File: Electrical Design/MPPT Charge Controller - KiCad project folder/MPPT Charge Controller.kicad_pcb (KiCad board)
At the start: 4 copper layers, 32 x 80 mm, 75 parts, among them J1 Conn_01x02_Socket, J2 Conn_01x02_Socket, J3 Conn_01x02_Socket, Q1 Q_Dual_NMOS_S1G1S2G2D2D2D1D1, Q2 Q_Dual_NMOS_S1G1S2G2D2D2D1D1, Q3 2N7002, U2 AP63203WU, U3 ACS712, U4 ACS712, U5 MCP4018

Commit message: update PCB for 140K R2
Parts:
- R2: value 499k -> 140K

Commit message: continue to adapt for MEGAphone
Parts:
- removed ? (x3): , 
- removed G***: LOGO, New Logo:byteSizedEngineeringLogo-5mm
- removed J1, J2, J3: Conn_01x02_Socket, TerminalBlock:TerminalBlock_bornier-2_P5.08mm
- removed J4: ~, Connector_PinSocket_2.54mm:PinSocket_1x02_P2.54mm_Vertical
- removed Q2: Q_Dual_NMOS_S1G1S2G2D2D2D1D1, Package_SO:PowerPAK_SO-8_Dual
- removed REF**: MountingHole_3.2mm_M3, MountingHole:MountingHole_3.2mm_M3
- removed TP1, TP10, TP11, TP12, TP13, TP2, TP3, TP4, TP5, TP6, TP7, TP8, TP9: TestPoint, TestPoint:TestPoint_Pad_D1.0mm
- removed TP14, TP15: TestPoint, TestPoint:TestPoint_Loop_D2.60mm_Drill1.6mm_Beaded
- added JP1: Jumper_2_Bridged, Jumper:SolderJumper-2_P1.3mm_Bridged_RoundedPad1.0x1.5mm, F.Cu at (103.1, 77.3)
- added JP2: Jumper_2_Bridged, Jumper:SolderJumper-2_P1.3mm_Bridged_RoundedPad1.0x1.5mm, F.Cu at (103.0, 111.9)
- added M2: ~, MegaCastle:MegaCastle2x23-Module-I30.0x53.6-M80000307FFFC, F.Cu at (110.4, 99.3)
- RSR1: value 0.02 -> 0.01
- moved D3 12.8 mm to (98.0, 119.8)
- moved D4 12.8 mm to (96.0, 119.7)
- moved R7 12.8 mm to (98.0, 119.8)
- moved R8 12.8 mm to (96.0, 119.7)
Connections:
- net Net-(J2-Pin_2) renamed VBAT_OUT
- net PWR GND renamed PWR_GND
- A1 pad 14: unconnected-(A1-RX/IO16-Pad14) -> UART_RX
- A1 pad 15: unconnected-(A1-TX/IO17-Pad15) -> UART_TX
- A1 pad 23: /Load Enable -> unconnected-(A1-D11-Pad23)
- R11 pad 2: +3.3V -> VCC_ACS712_2
- R14 pad 2: +3.3V -> VCC_ACS712
- U3 pad 8: +3.3V -> VCC_ACS712
- U4 pad 8: +3.3V -> VCC_ACS712_2
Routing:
- net +3.3V: track 83.5 -> 139.6 mm
- net VBAT_OUT: track 1.91 -> 56.7 mm
- net UART_RX: track 0.00 -> 47.1 mm, vias 0 -> 1
- net UART_TX: track 0.00 -> 34.9 mm, vias 0 -> 2
- net /Load Enable: track 21.6 -> 0.00 mm, vias 2 -> 0
- net /STAT2: track 97.3 -> 77.3 mm, vias 6 -> 4
- net PWR_GND: track 16.2 -> 33.3 mm
- net /STAT1: track 88.0 -> 73.6 mm, vias 6 -> 2
- net /~{Charge EN}: track 19.3 -> 27.6 mm
- net /VREF: track 55.3 -> 47.4 mm, vias 7 -> 5
- net /HIDRV: track 23.6 -> 30.0 mm, vias 3 -> 2
- net /MPPSET: track 31.6 -> 37.4 mm, vias 4 -> 3
- net /LODRV: track 22.4 -> 28.2 mm, vias 3 -> 2
- net /BTST: track 22.2 -> 28.0 mm, vias 4 -> 3
- net /RGEN: track 20.0 -> 25.6 mm, vias 5 -> 4
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- removed copper zone on F.Cu, net Net-(J3-Pin_1)
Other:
- board size 32 x 80 mm -> 35.6 x 58.4 mm
- board text added: "3.3V OUT"
- board text added: "BATTERY (LiFePO4 1S)"
- board text added: "PWR GND"
- board text added: "UART RX"
- board text added: "UART TX"
- board text removed: "- + 12V Battery"
- board text removed: "- + 12V Load"
- board text removed: "- + 5V-28V Solar Input"

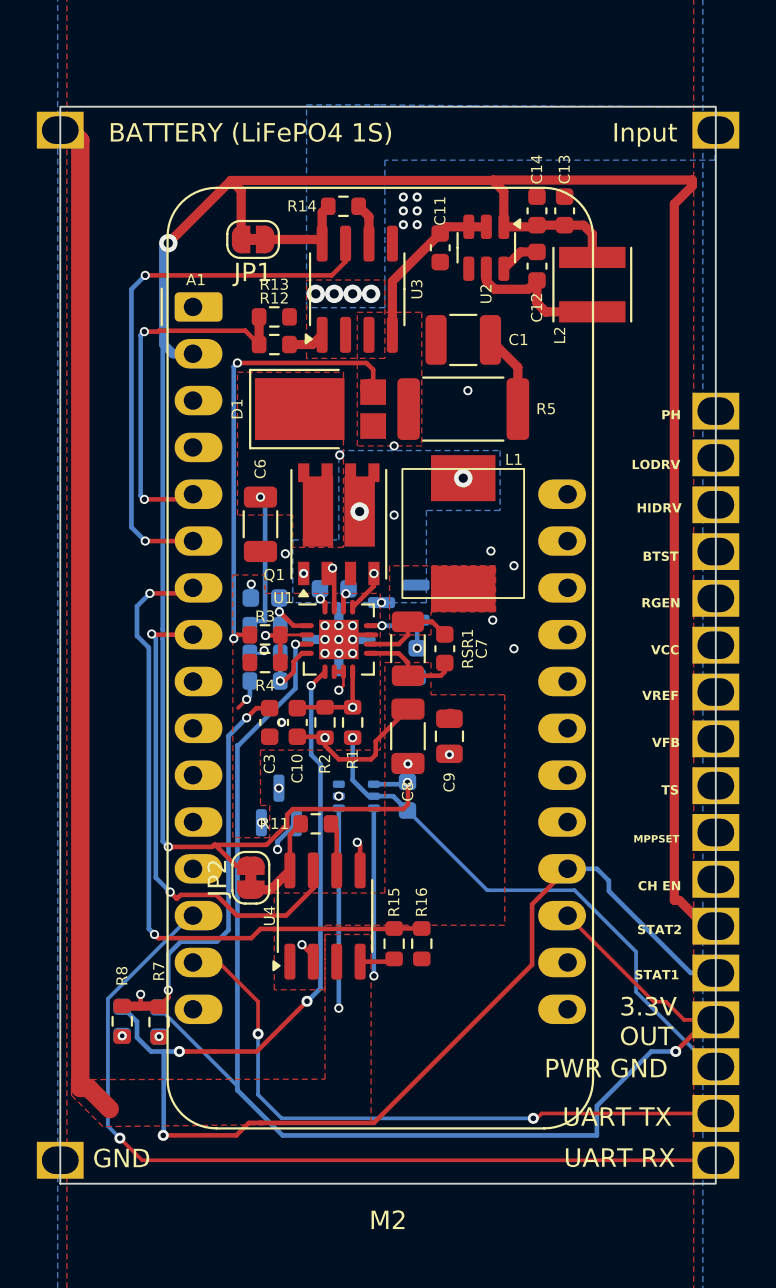
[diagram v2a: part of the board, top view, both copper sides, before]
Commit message: resolve most DRC violations
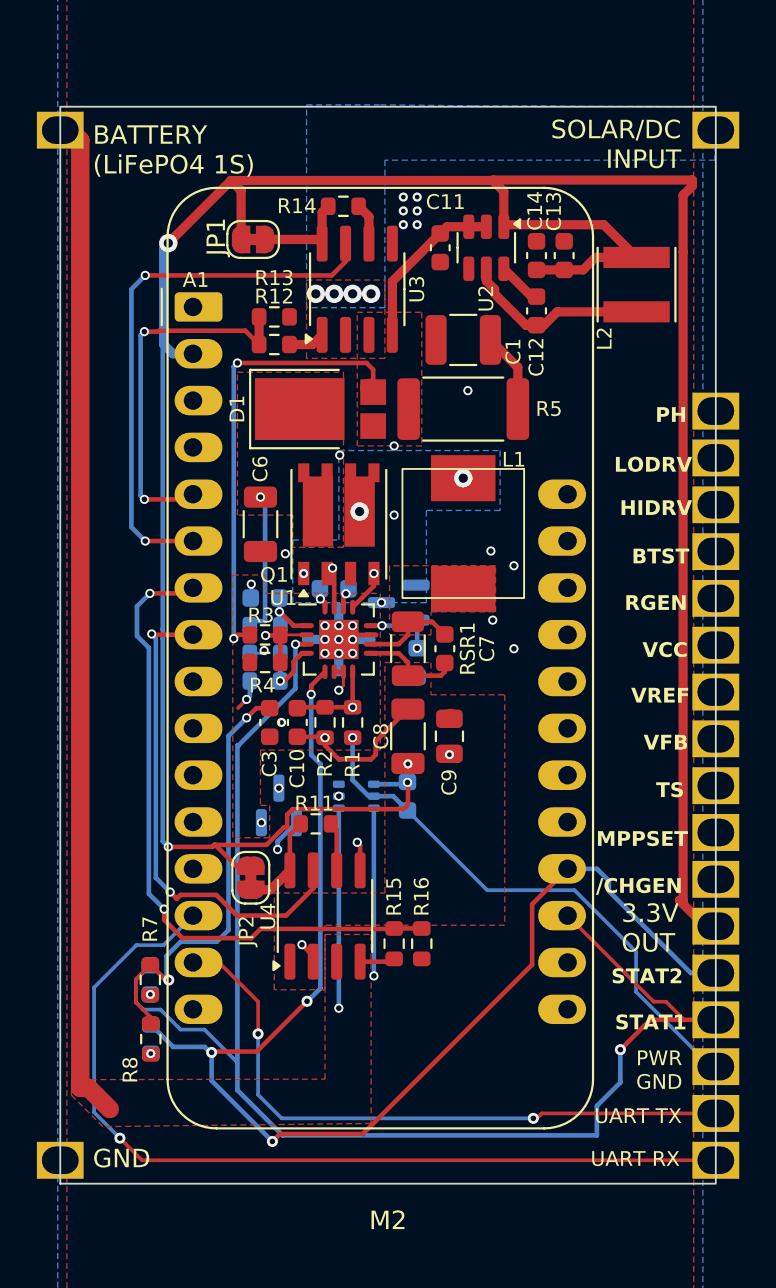
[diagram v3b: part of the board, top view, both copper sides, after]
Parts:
- R5: value 2 -> 2 Ohm
- moved C12 2.43 mm to (118.5, 81.2)
- moved C13 2.43 mm to (120.0, 78.2)
- moved C14 2.43 mm to (118.5, 78.2)
- moved L2 2.40 mm to (123.9, 79.8)
- moved D3 2.34 mm to (97.5, 117.5)
- moved R7 2.34 mm to (97.5, 117.5)
- moved D4 1.82 mm to (97.5, 120.7)
- moved R8 1.82 mm to (97.5, 120.7)
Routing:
- net +3.3V: track 139.6 -> 147.2 mm
- net /STAT2: track 77.3 -> 70.1 mm
- net /STAT1: track 73.6 -> 79.1 mm
- net Net-(U2-SW): track 8.24 -> 10.3 mm
- net UART_RX: track 47.1 -> 48.6 mm
- net /VREF: track 47.4 -> 48.5 mm, vias 5 -> 4
- net /Battery Voltage: track 36.4 -> 35.7 mm
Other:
- board text added: "/CHGEN"
- board text added: "SOLAR/DC INPUT"
- board text removed: "CH EN"
- board text removed: "Input"

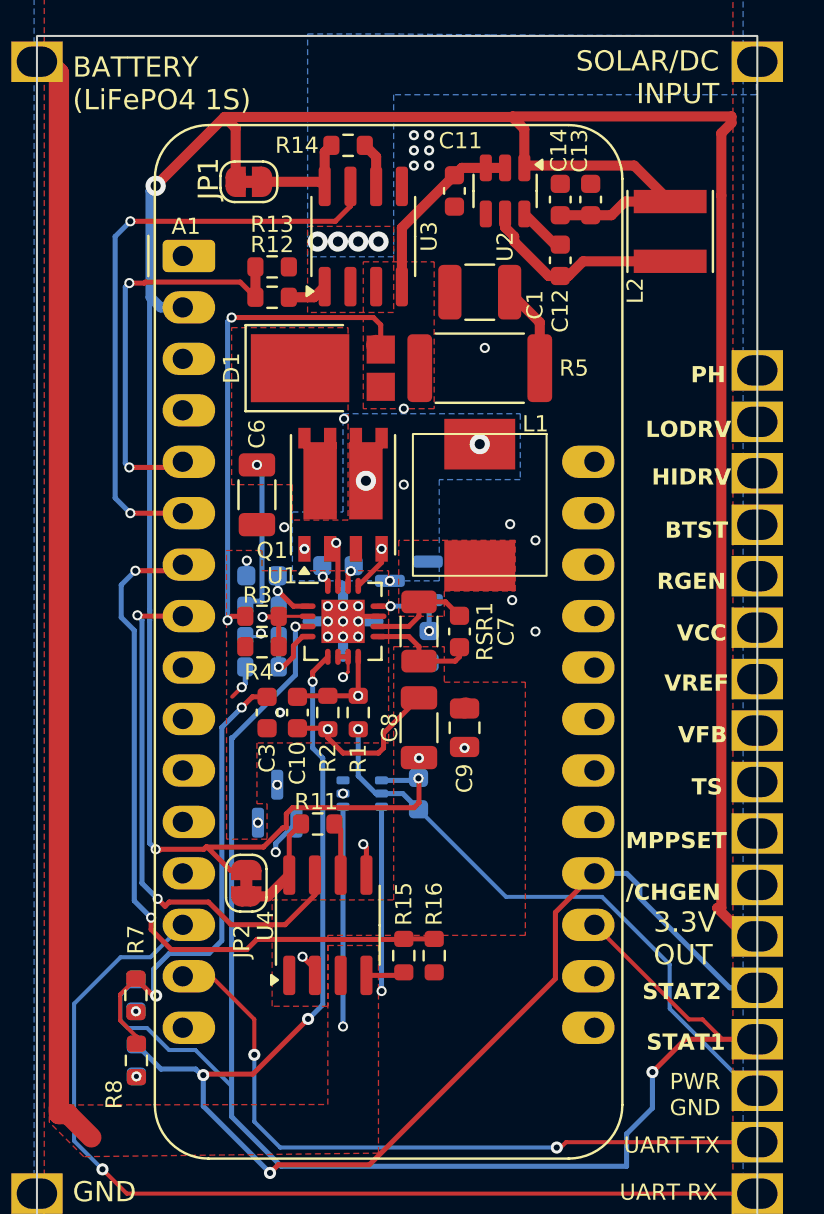
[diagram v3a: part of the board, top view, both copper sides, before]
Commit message: add silkscreen for all component values
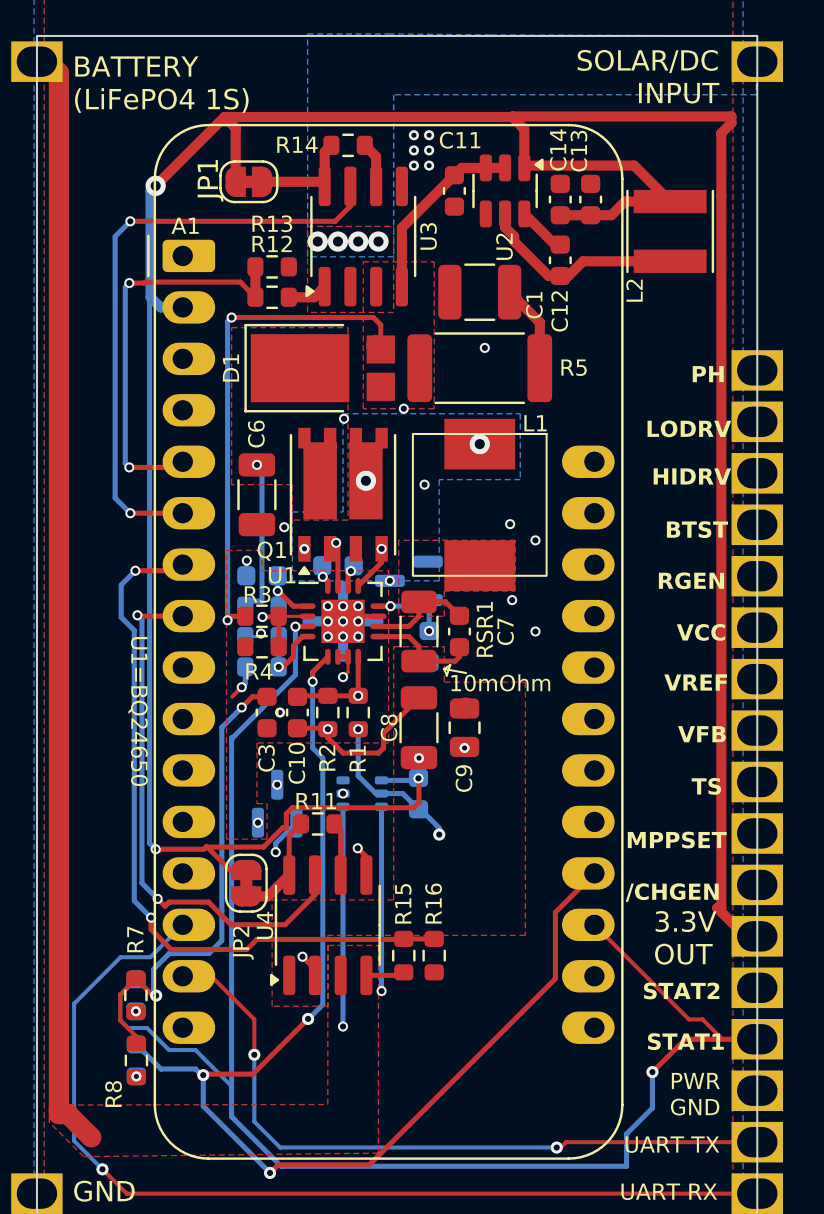
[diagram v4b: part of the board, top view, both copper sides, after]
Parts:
- C2: value 1uF -> C2=1uF
- Q1: value Q_Dual_NMOS_S1G1S2G2D2D2D1D1 -> SI7272DP
- R10: value 30.1k -> R10=30.1k
- R6: value 10 -> R6=10
- R9: value 5.23k -> R9=5.23k
- RSR1: value 0.01 -> 10mOhm
- U3, U4: value ACS712 -> ACS712-20A
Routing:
- net PWR_GND: track 33.3 -> 32.7 mm, vias 13 -> 14
- net /BTST: track 28.0 -> 27.4 mm
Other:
- board text added: "U1=BQ24650"

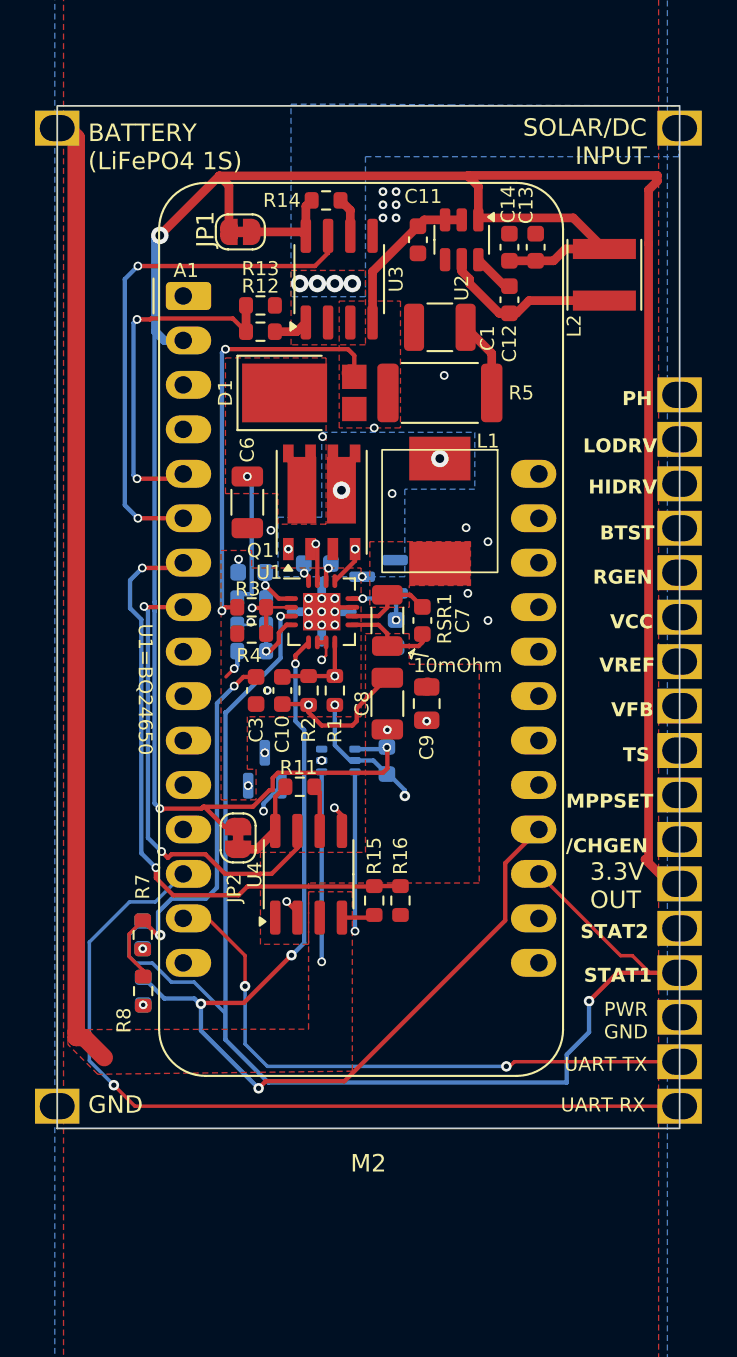
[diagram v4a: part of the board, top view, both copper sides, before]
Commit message: switch to panelised footprint
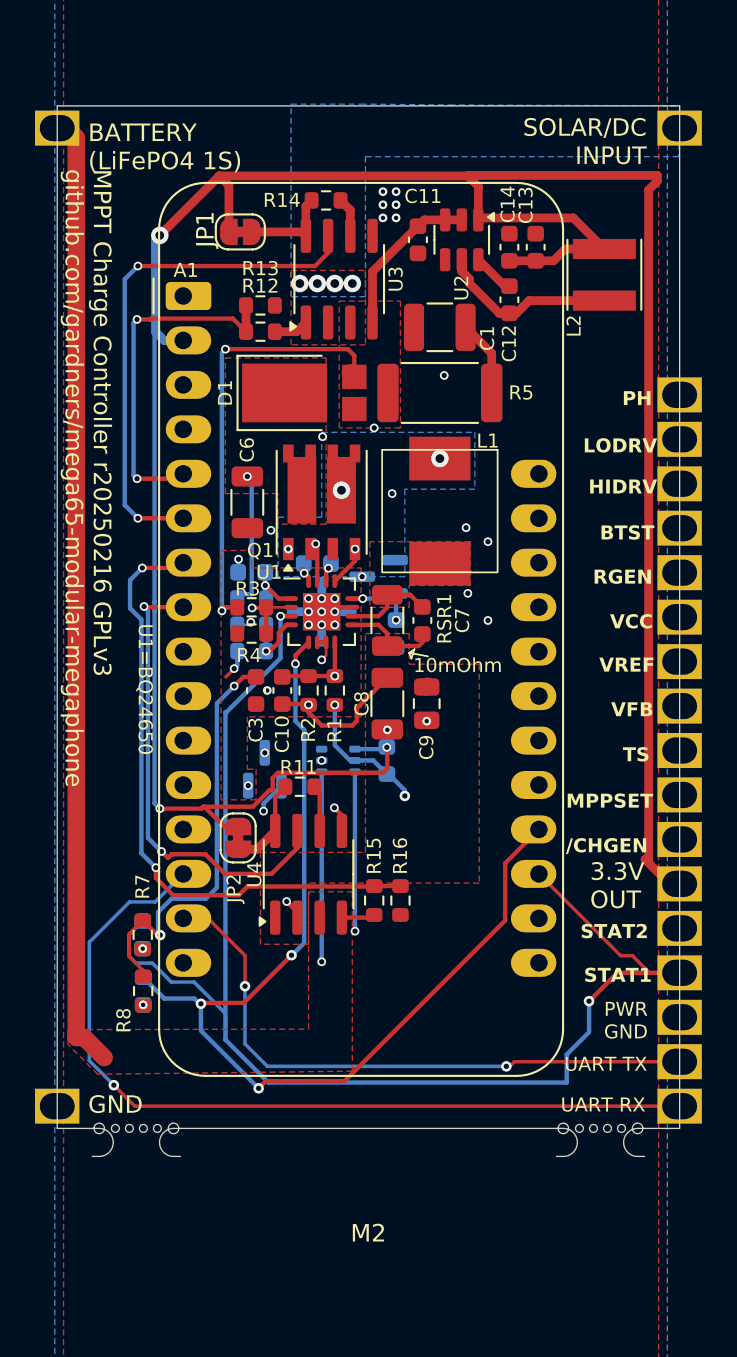
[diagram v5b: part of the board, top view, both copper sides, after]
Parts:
- M2: footprint MegaCastle:MegaCastle2x23-Module-I30.0x53.6-M80000307FFFC -> MegaCastle:MegaCastle2x23-Module-I30.0x53.6-M80000307FFFC-PANEL
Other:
- board size 35.6 x 58.4 mm -> 35.6 x 60 mm
- board text added: "${TITLE} r20250216 GPLv3 github.com/gardners/mega65-modular-megaphone"
- board text removed: "${TITLE} REV:${REVISION}"

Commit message: finish panelising
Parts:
- added A1: Adafruit_Feather_HUZZAH32_ESP32, Module:Adafruit_Feather, F.Cu at (157.2, 98.5)
- added C1: 2.2uF, Capacitor_SMD:C_1210_3225Metric, F.Cu at (161.7, 81.2)
- added C10: 22pF, Capacitor_SMD:C_0603_1608Metric, F.Cu at (152.7, 102.0)
- added C11: 10uF, Capacitor_SMD:C_0603_1608Metric, F.Cu at (160.5, 76.2)
- added C12: 0.1uF, Capacitor_SMD:C_0603_1608Metric, F.Cu at (165.7, 79.6)
- added C13: 22uF, Capacitor_SMD:C_0603_1608Metric, F.Cu at (167.2, 76.6)
- added C14: 22uF, Capacitor_SMD:C_0603_1608Metric, F.Cu at (165.7, 76.6)
- added C15: 0.1uF, Capacitor_SMD:C_0603_1608Metric, B.Cu at (158.7, 106.0)
- added C2: C2=1uF, Capacitor_SMD:C_0603_1608Metric, B.Cu at (151.0, 95.2)
- added C3: 1uF, Capacitor_SMD:C_0603_1608Metric, F.Cu at (151.2, 102.0)
- added C4: 1uF, Capacitor_SMD:C_0603_1608Metric, B.Cu at (159.2, 98.7)
- added C5: 0.1uF, Capacitor_SMD:C_0603_1608Metric, B.Cu at (154.7, 94.7)
- added C6: 10uF, Capacitor_SMD:C_1206_3216Metric, F.Cu at (150.7, 91.2)
- added C7: 0.1uF, Capacitor_SMD:C_0603_1608Metric, F.Cu at (160.7, 98.0)
- added C8: 10uF, Capacitor_SMD:C_1206_3216Metric, F.Cu at (158.7, 102.7)
- added C9: 4.7uF, Capacitor_SMD:C_0805_2012Metric, F.Cu at (161.0, 102.7)
- added D1: PDS1040, Diode_SMD:D_PowerDI-5, F.Cu at (154.0, 85.0)
- added D2: BAT54C, Package_TO_SOT_SMD:SOT-23, B.Cu at (158.2, 95.5)
- added D3: RED, LED_SMD:LED_0603_1608Metric, B.Cu at (144.8, 115.9)
- added D4: GREEN, LED_SMD:LED_0603_1608Metric, B.Cu at (144.8, 119.1)
- added JP1: Jumper_2_Bridged, Jumper:SolderJumper-2_P1.3mm_Bridged_RoundedPad1.0x1.5mm, F.Cu at (150.3, 75.8)
- added JP2: Jumper_2_Bridged, Jumper:SolderJumper-2_P1.3mm_Bridged_RoundedPad1.0x1.5mm, F.Cu at (150.2, 110.4)
- added L1: 10uH, MPPT Charge Controller Footprint Library:L_Vishay_6.9x6.5, F.Cu at (161.7, 91.7)
- added L2: 4.7uH, Inductor_SMD:L_Vishay_IFSC-1515AH_4x4x1.8mm, F.Cu at (171.1, 78.2)
- added M2: ~, MegaCastle:MegaCastle2x23-Module-I30.0x53.6-M80000307FFFC-PANEL, F.Cu at (157.6, 97.8)
- added NT1: ~, NetTie:NetTie-2_SMD_Pad0.5mm, B.Cu at (156.2, 97.5)
- added NT2: ~, NetTie:NetTie-2_SMD_Pad0.5mm, B.Cu at (155.0, 96.2)
- added NT3: ~, NetTie:NetTie-2_SMD_Pad0.5mm, B.Cu at (153.7, 97.5)
- added NT4: ~, NetTie:NetTie-2_SMD_Pad0.5mm, B.Cu at (155.0, 98.7)
- added Q1: SI7272DP, Package_SO:PowerPAK_SO-8_Dual, F.Cu at (155.0, 91.2)
- added Q3: 2N7002, Package_TO_SOT_SMD:SOT-23, B.Cu at (151.7, 106.5)
- added R1: 100k, Resistor_SMD:R_0603_1608Metric, F.Cu at (155.7, 102.0)
- added R10: R10=30.1k, Resistor_SMD:R_0603_1608Metric, B.Cu at (151.0, 99.7)
- added R11: 100k, Resistor_SMD:R_0603_1608Metric, F.Cu at (153.7, 107.5)
- added R12: 499k, Resistor_SMD:R_0603_1608Metric, F.Cu at (151.5, 81.5)
- added R13: 36k, Resistor_SMD:R_0603_1608Metric, F.Cu at (151.5, 80.0)
- added R14: 100k, Resistor_SMD:R_0603_1608Metric, F.Cu at (155.2, 74.0)
- added R15: 499k, Resistor_SMD:R_0603_1608Metric, F.Cu at (158.0, 114.0)
- added R16: 100k, Resistor_SMD:R_0603_1608Metric, F.Cu at (159.5, 114.0)
- added R2: 140K, Resistor_SMD:R_0603_1608Metric, F.Cu at (154.2, 102.0)
- added R3: 499k, Resistor_SMD:R_0603_1608Metric, F.Cu at (151.0, 97.2)
- added R4: DNP, Resistor_SMD:R_0603_1608Metric, F.Cu at (151.0, 98.7)
- added R5: 2 Ohm, Resistor_SMD:R_2512_6332Metric, F.Cu at (161.7, 85.0)
- added R6: R6=10, Resistor_SMD:R_0603_1608Metric, B.Cu at (151.0, 96.7)
- added R7: 100, Resistor_SMD:R_0603_1608Metric, F.Cu at (144.8, 115.9)
- added R8: 100, Resistor_SMD:R_0603_1608Metric, F.Cu at (144.8, 119.1)
- added R9: R9=5.23k, Resistor_SMD:R_0603_1608Metric, B.Cu at (151.0, 98.2)
- added RSR1: 10mOhm, Resistor_SMD:R_1206_3216Metric, F.Cu at (158.7, 98.0)
- added U1: ~, MPPT Charge Controller Footprint Library:VQFN-16_EP_3.5x3.5_Pitch0.5mm, F.Cu at (155.0, 97.5)
- added U2: AP63203WU, Package_TO_SOT_SMD:TSOT-23-6, F.Cu at (163.0, 76.2)
- added U3: ACS712-20A, Package_SO:SOIC-8_3.9x4.9mm_P1.27mm, F.Cu at (156.0, 78.5)
- added U4: ACS712-20A, Package_SO:SOIC-8_3.9x4.9mm_P1.27mm, F.Cu at (154.2, 112.5)
- added U5: MCP4018, Package_TO_SOT_SMD:SOT-363_SC-70-6, B.Cu at (155.9, 106.0)
- moved D3 1.56 mm to (97.4, 115.9)
- moved R7 1.56 mm to (97.4, 115.9)
- moved A1 1.56 mm to (109.9, 98.5)
- moved C1 1.56 mm to (114.4, 81.2)
- moved C10 1.56 mm to (105.4, 102.0)
- moved C11 1.56 mm to (113.1, 76.2)
- moved C12 1.56 mm to (118.3, 79.6)
- moved C13 1.56 mm to (119.8, 76.6)
- moved C14 1.56 mm to (118.3, 76.6)
- moved C15 1.56 mm to (111.3, 106.0)
- moved C2 1.56 mm to (103.6, 95.2)
- moved C3 1.56 mm to (103.9, 102.0)
- moved C4 1.56 mm to (111.9, 98.7)
- moved C5 1.56 mm to (107.4, 94.7)
- moved C6 1.56 mm to (103.4, 91.2)
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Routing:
- net +3.3V: track 147.2 -> 294.5 mm, vias 3 -> 6
- net /STAT1: track 79.1 -> 158.2 mm, vias 2 -> 4
- net /STAT2: track 69.8 -> 139.5 mm, vias 4 -> 8
- net VBAT_OUT: track 56.7 -> 113.4 mm
- net UART_RX: track 48.6 -> 97.1 mm, vias 1 -> 2
- net /VREF: track 48.5 -> 97.1 mm, vias 4 -> 8
- net /MPPSET: track 37.4 -> 74.8 mm, vias 3 -> 6
- net /Battery Voltage: track 35.7 -> 71.4 mm, vias 2 -> 4
- net UART_TX: track 34.9 -> 69.9 mm, vias 2 -> 4
- net /VCC: track 34.8 -> 69.5 mm, vias 4 -> 8
- net /VIN: track 34.3 -> 68.5 mm, vias 2 -> 4
- net PWR_GND: track 32.7 -> 65.4 mm, vias 14 -> 28
- net /TS: track 31.1 -> 62.2 mm, vias 2 -> 4
- net /HIDRV: track 30.0 -> 59.9 mm, vias 2 -> 4
- net /Solar Current: track 29.8 -> 59.5 mm, vias 2 -> 4
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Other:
- outline, holes or cut-outs redrawn
- board text added: "P1"
- board text added: "P2"
